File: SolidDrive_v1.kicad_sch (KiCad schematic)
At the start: 21 parts, among them J1 Batt, M1 Motor_DC, Q1 NMOS, Q2 NMOS, Q3 NMOS, Q4 NMOS, U1 LM7805_TO220, U2 TLP250, U3 TLP250, U4 TLP250, U5 TLP250

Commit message: [update] complete power cuircuit
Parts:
- added C3, C4, C5, C6: 0.1μF, Capacitor_THT:C_Disc_D3.0mm_W1.6mm_P2.50mm, symbol Device:C
- added C7, C8: 470μF, Capacitor_THT:CP_Radial_D5.0mm_P2.00mm, symbol Device:C_Polarized
- added D1, D2, D3, D4: 1N4007, Diode_THT:D_DO-41_SOD81_P10.16mm_Horizontal, symbol Diode:1N4007
- R1, R2, R3, R4, R5, R6, R7, R8: footprint (none) -> Resistor_THT:R_Axial_DIN0207_L6.3mm_D2.5mm_P10.16mm_Horizontal
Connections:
- net +12V: now also D1.2 (A), D2.2 (A), D3.2 (A), D4.2 (A)
- net +BATT: now also J1.1 (Pin_1), C7.1, C8.1; no longer J1.2 (Pin_2)
- net GND: now also U2.3 (C), U3.3 (C), U4.3 (C), U5.3 (C); no longer C1.2, C2.2, J1.1 (Pin_1), Q3.3 (S), Q4.3 (S), R3.1, R4.2, U1.2 (GND)
- net at R8.1: now also U4.6 (VO), U4.7 (VO)
- net at M1.1 (+), Q1.3 (S), Q3.1 (D)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: now also U2.5 (VEE), C3.2
- net at M1.2 (-), Q2.3 (S), Q4.1 (D)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: now also U4.5 (VEE), C4.2
- net at U4.8 (VCC): now also C4.1, D2.1 (K)
- net at R5.2: now also U2.6 (VO), U2.7 (VO)
- net at U2.8 (VCC): now also C3.1, D1.1 (K)
- net at R7.1: now also U5.6 (VO), U5.7 (VO)
- net GNDPWR: now reaches U3.5 (VEE)
- net GNDPWR: now also C1.2, C2.2, J1.2 (Pin_2), Q3.3 (S), Q4.3 (S), R3.1, R4.2, U1.2 (GND), U5.5 (VEE), C5.2, C6.2, C7.2, C8.2
- net at U3.6 (VO): now also R6.2, U3.7 (VO)
- net at U3.8 (VCC): now also C5.1, D3.1 (K)
- net at U5.8 (VCC): now also C6.1, D4.1 (K)
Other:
- moved on the sheet: J1

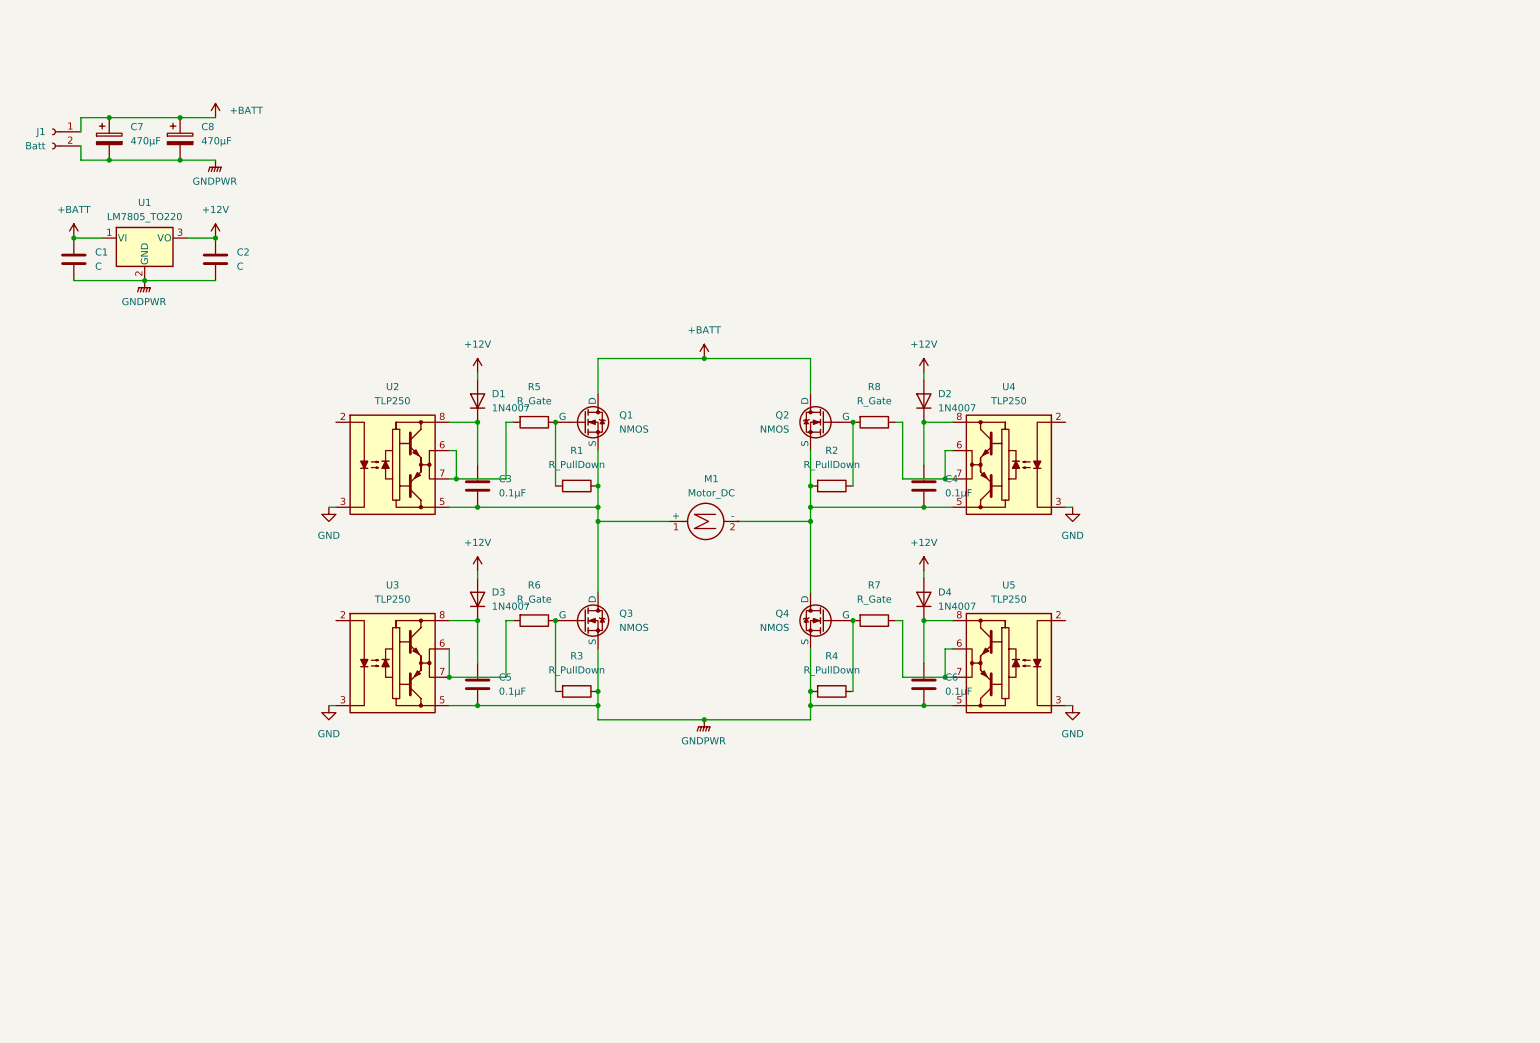
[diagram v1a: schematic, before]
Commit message: [update] complete logic circuit
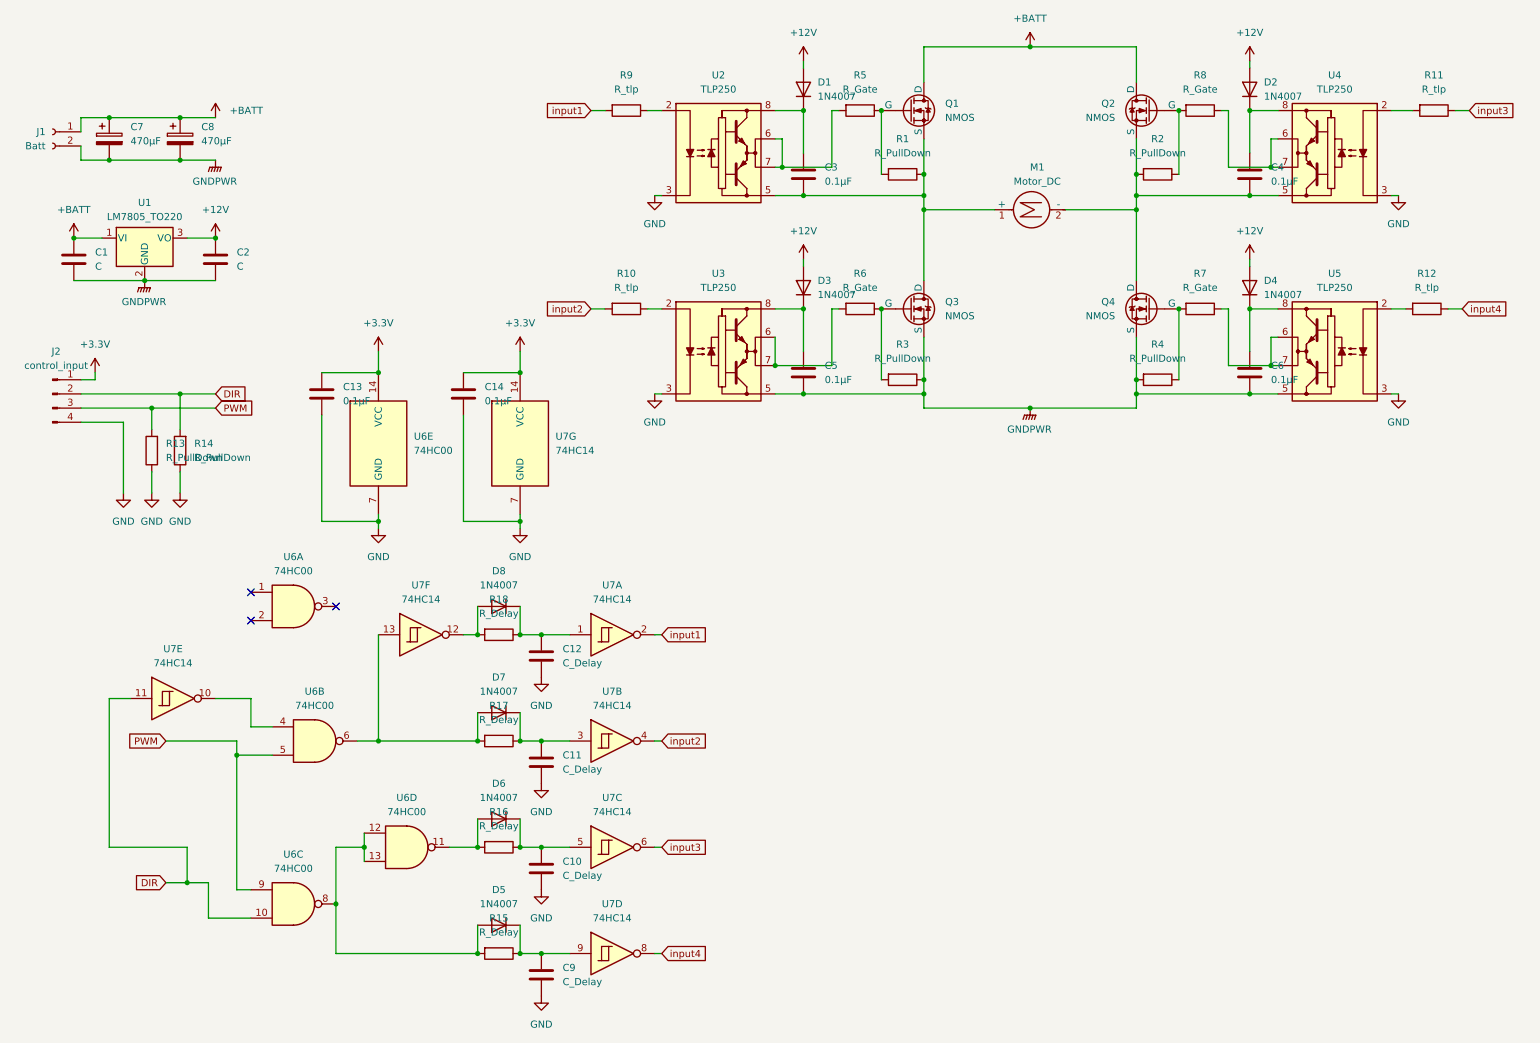
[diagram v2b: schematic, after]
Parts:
- added C10, C11, C12, C9: C_Delay, Capacitor_THT:C_Disc_D3.0mm_W1.6mm_P2.50mm, symbol Device:C
- added C13, C14: 0.1μF, Capacitor_THT:C_Disc_D3.0mm_W1.6mm_P2.50mm, symbol Device:C
- added D5, D6, D7, D8: 1N4007, Diode_THT:D_DO-41_SOD81_P10.16mm_Horizontal, symbol Diode:1N4007
- added J2: control_input, Connector_PinHeader_2.54mm:PinHeader_1x04_P2.54mm_Horizontal, symbol Connector:Conn_01x04_Pin
- added R10, R11, R12, R9: R_tlp, Resistor_THT:R_Axial_DIN0207_L6.3mm_D2.5mm_P10.16mm_Horizontal, symbol Device:R
- added R13, R14: R_PullDown, Resistor_THT:R_Axial_DIN0207_L6.3mm_D2.5mm_P10.16mm_Horizontal, symbol Device:R
- added R15, R16, R17, R18: R_Delay, Resistor_THT:R_Axial_DIN0207_L6.3mm_D2.5mm_P10.16mm_Horizontal, symbol Device:R
- added U6: 74HC00, Package_DIP:DIP-14_W7.62mm, symbol 74xx:74HC00
- added U7: 74HC14, Package_DIP:DIP-14_W7.62mm, symbol 74xx:74HC14
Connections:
- net GND: now also C10.2, C11.2, C12.2, C13.2, C14.2, C9.2, J2.4 (Pin_4), R13.1, R14.1, U6.7 (GND), U7.7 (GND)
- net at U4.2 (A): now also R11.2
- net at U2.2 (A): now also R9.1
- net at U3.2 (A): now also R10.1
- net at U5.2 (A): now also R12.2
- new net: C12.1, D8.1 (K), R18.1, U7.1
- new net: C9.1, D5.1 (K), R15.1, U7.9
- new net: D8.2 (A), R18.2, U7.12
- new net: D7.2 (A), R17.2, U6.6, U7.13
- new net: C10.1, D6.1 (K), R16.1, U7.5
- new net: D6.2 (A), R16.2, U6.11
- new net: U6.4, U7.10
- new net: D5.2 (A), R15.2, U6.12, U6.13, U6.8
- new net: C11.1, D7.1 (K), R17.1, U7.3
- new net +3.3V: C13.1, C14.1, J2.1 (Pin_1), U6.14 (VCC), U7.14 (VCC)
- new net DIR: J2.2 (Pin_2), R14.2, U6.10, U7.11
- new net PWM: J2.3 (Pin_3), R13.2, U6.5, U6.9
- new net input1: R9.2, U7.2
- new net input2: R10.2, U7.4
- new net input3: R11.1, U7.6
- new net input4: R12.1, U7.8
- no-connect marks 0 -> 3
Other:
- moved on the sheet: C3, C4, C5, C6, D1, D2, D3, D4, M1, Q1, Q2, Q3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

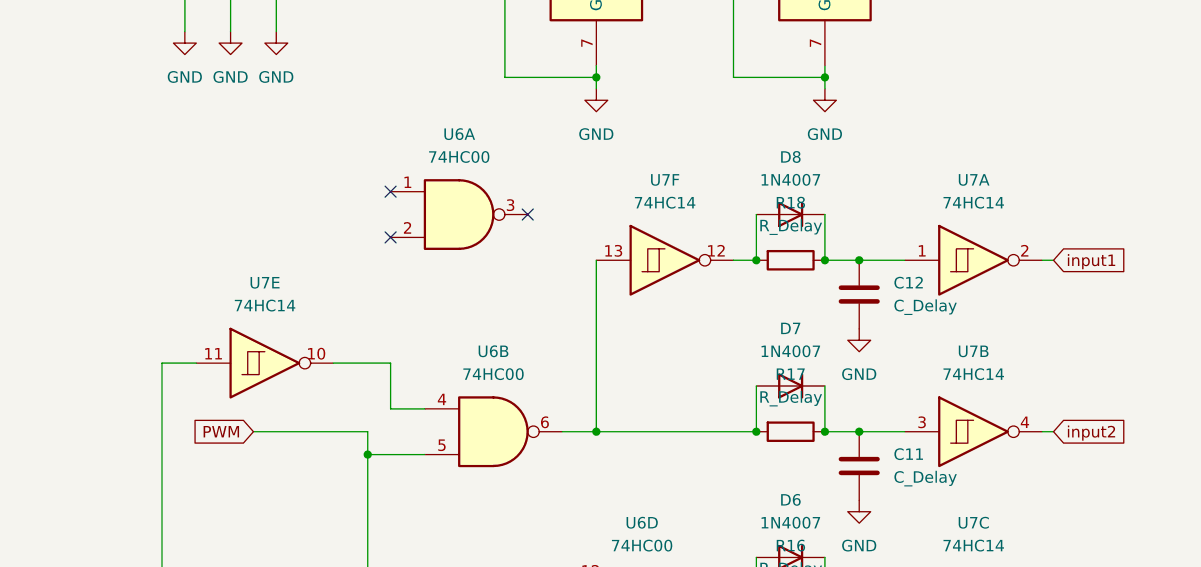
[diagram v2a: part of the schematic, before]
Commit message: [update] complete logic circuit placement
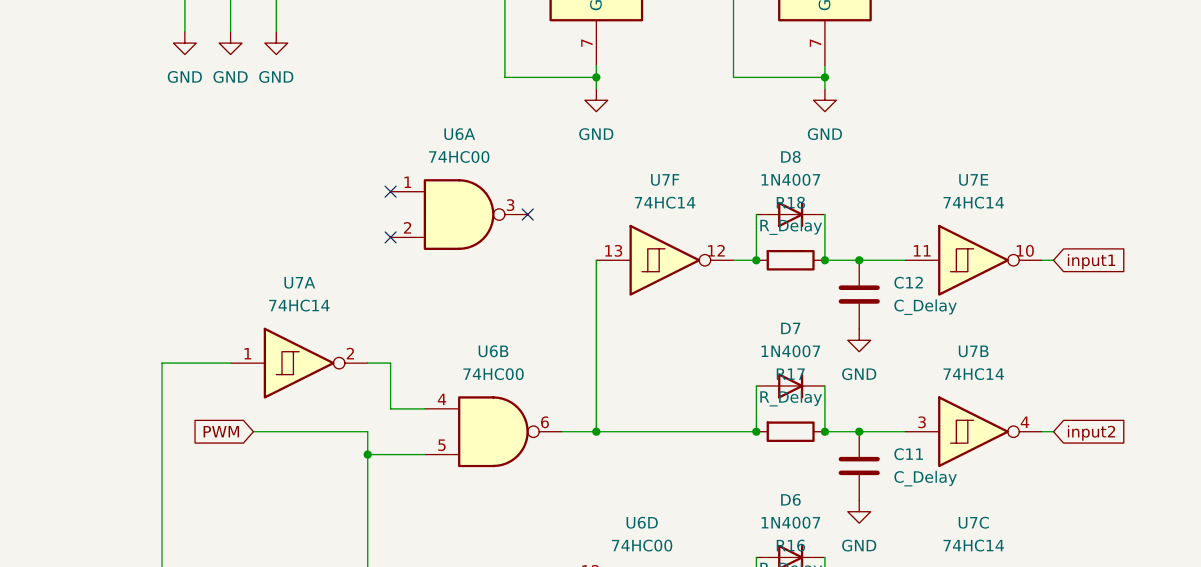
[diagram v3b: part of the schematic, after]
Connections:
- net DIR: now also U7.1; no longer U7.11
- net input1: now also U7.10; no longer U7.2
- net at C12.1, D8.1 (K), R18.1: now also U7.11; no longer U7.1
- net at U6.4: now also U7.2; no longer U7.10
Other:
- moved on the sheet: U7A, U7E
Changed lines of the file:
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@@
 	)
 	(junction
-		(at 40.64 34.29)
+		(at 105.41 127)
 		(diameter 0)
 		(color 0 0 0 0)
 	)
 	(junction
-		(at 105.41 127)
+		(at 40.64 34.29)
 		(diameter 0)
 		(color 0 0 0 0)
@@
 	(wire
 		(pts
-			(xy 31.75 138.43) (xy 27.94 138.43)
-		)
-		(stroke
-			(width 0)
-			(type default)
-		)
-	)
-	(wire
-		(pts
 			(xy 228.6 78.74) (xy 236.22 78.74)
 		)
@@
 	(wire
 		(pts
+			(xy 27.94 138.43) (xy 35.56 138.43)
+		)
+		(stroke
+			(width 0)
+			(type default)
+		)
+	)
+	(wire
+		(pts
 			(xy 157.48 68.58) (xy 157.48 78.74)
 		)
@@
 	(wire
 		(pts
+			(xy 50.8 138.43) (xy 53.34 138.43)
+		)
+		(stroke
+			(width 0)
+			(type default)
+		)
+	)
+	(wire
+		(pts
 			(xy 22.86 86.36) (xy 35.56 86.36)
 		)
@@
 	(wire
 		(pts
+			(xy 105.41 127) (xy 110.49 127)
+		)
+		(stroke
+			(width 0)
+			(type default)
+		)
+	)
+	(wire
+		(pts
 			(xy 257.81 83.82) (xy 259.08 83.82)
 		)
@@
 	(wire
 		(pts
+			(xy 125.73 127) (xy 127 127)
+		)
+		(stroke
+			(width 0)
+			(type default)
+		)
+	)
+	(wire
+		(pts
 			(xy 124.46 33.02) (xy 127 33.02)
 		)
@@
 	(wire
 		(pts
-			(xy 125.73 127) (xy 127 127)
-		)
-		(stroke
-			(width 0)
-			(type default)
-		)
-	)
-	(wire
-		(pts
 			(xy 236.22 78.74) (xy 237.49 78.74)
 		)
@@
 	(wire
 		(pts
-			(xy 46.99 138.43) (xy 53.34 138.43)
-		)
-		(stroke
-			(width 0)
-			(type default)
-		)
-	)
-	(wire
-		(pts
 			(xy 147.32 73.66) (xy 147.32 78.74)
 		)
@@
 	(wire
 		(pts
-			(xy 105.41 127) (xy 110.49 127)
-		)
-		(stroke
-			(width 0)
-			(type default)
-		)
-	)
-	(wire
-		(pts
 			(xy 38.1 171.45) (xy 41.91 171.45)
 		)
@@
 	(symbol
 		(lib_id "74xx:74HC14")
-		(at 118.11 127 0)
+		(at 43.18 138.43 0)
 		(unit 1)
 		(exclude_from_sim no)
@@
 		(fields_autoplaced yes)
 		(property "Reference" "U7"
-			(at 118.11 118.11 0)
+			(at 43.18 129.54 0)
 			(effects
 				(font
@@
 		)
 		(property "Value" "74HC14"
-			(at 118.11 120.65 0)
+			(at 43.18 132.08 0)
 			(effects
 				(font
@@
 		)
 		(property "Footprint" "Package_DIP:DIP-14_W7.62mm"
-			(at 118.11 127 0)
+			(at 43.18 138.43 0)
 			(effects
 				(font
@@
 		)
 		(property "Datasheet" "http://www.ti.com/lit/gpn/sn74HC14"
-			(at 118.11 127 0)
+			(at 43.18 138.43 0)
 			(effects
 				(font
@@
 		)
 		(property "Description" "Hex inverter schmitt trigger"
-			(at 118.11 127 0)
+			(at 43.18 138.43 0)
 			(effects
 				(font
@@
 	(symbol
 		(lib_id "74xx:74HC14")
-		(at 39.37 138.43 0)
+		(at 118.11 127 0)
 		(unit 5)
 		(exclude_from_sim no)
@@
 		(fields_autoplaced yes)
 		(property "Reference" "U7"
-			(at 39.37 129.54 0)
+			(at 118.11 118.11 0)
 			(effects
 				(font
@@
 		)
 		(property "Value" "74HC14"
-			(at 39.37 132.08 0)
+			(at 118.11 120.65 0)
 			(effects
 				(font
@@
 		)
 		(property "Footprint" "Package_DIP:DIP-14_W7.62mm"
-			(at 39.37 138.43 0)
+			(at 118.11 127 0)
 			(effects
 				(font
@@
 		)
 		(property "Datasheet" "http://www.ti.com/lit/gpn/sn74HC14"
-			(at 39.37 138.43 0)
+			(at 118.11 127 0)
 			(effects
 				(font
@@
 		)
 		(property "Description" "Hex inverter schmitt trigger"
-			(at 39.37 138.43 0)
+			(at 118.11 127 0)
 			(effects
 				(font

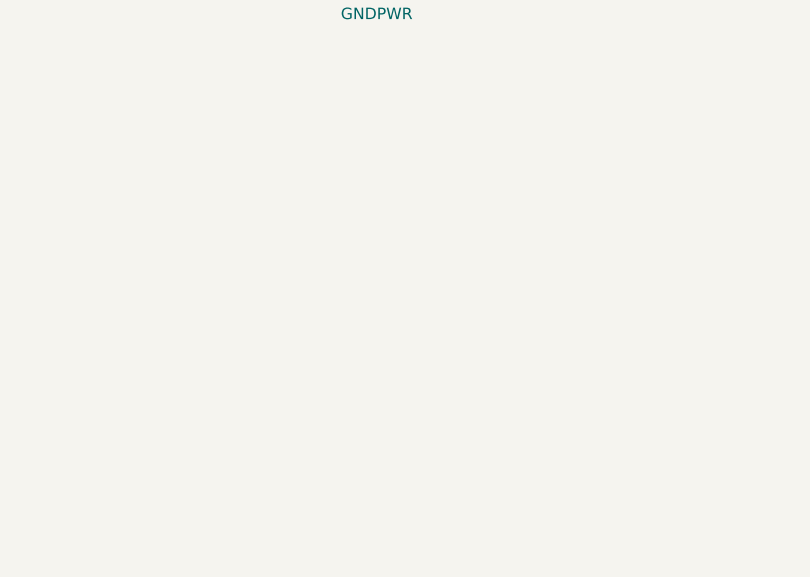
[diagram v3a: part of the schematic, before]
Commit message: [udpate] complete part position
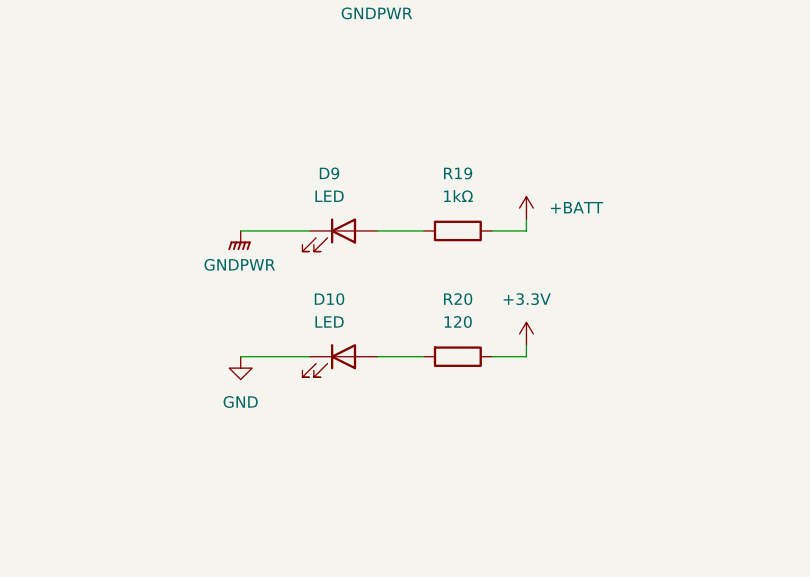
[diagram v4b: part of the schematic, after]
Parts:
- added D10, D9: LED, LED_THT:LED_D3.0mm, symbol Device:LED
- added R19: 1kΩ, Resistor_THT:R_Axial_DIN0207_L6.3mm_D2.5mm_P10.16mm_Horizontal, symbol Device:R
- added R20: 120, Resistor_THT:R_Axial_DIN0207_L6.3mm_D2.5mm_P10.16mm_Horizontal, symbol Device:R
- C7, C8: footprint Capacitor_THT:CP_Radial_D5.0mm_P2.00mm -> Capacitor_THT:CP_Radial_D10.0mm_P7.50mm
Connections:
- net +3.3V: now also R20.1
- net +BATT: now also R19.1
- net GND: now also D10.1 (K)
- net GNDPWR: now also D9.1 (K)
- new net: D9.2 (A), R19.2
- new net: D10.2 (A), R20.2
